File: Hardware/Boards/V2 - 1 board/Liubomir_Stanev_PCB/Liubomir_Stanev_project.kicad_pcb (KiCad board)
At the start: 2 copper layers, 145.5 x 73.5 mm, 30 parts, among them J1 Conn_01x03_Pin, J2 Conn_01x03_Pin, J3 Conn_01x02_Pin, J4 Conn_01x03_Pin, J5 Conn_01x03_Pin, J6 Conn_01x02_Pin, U1 GY-8511 UV sensor, U2 TEMT6000, U3 DS18B20-air, U4 Turbidity sensor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

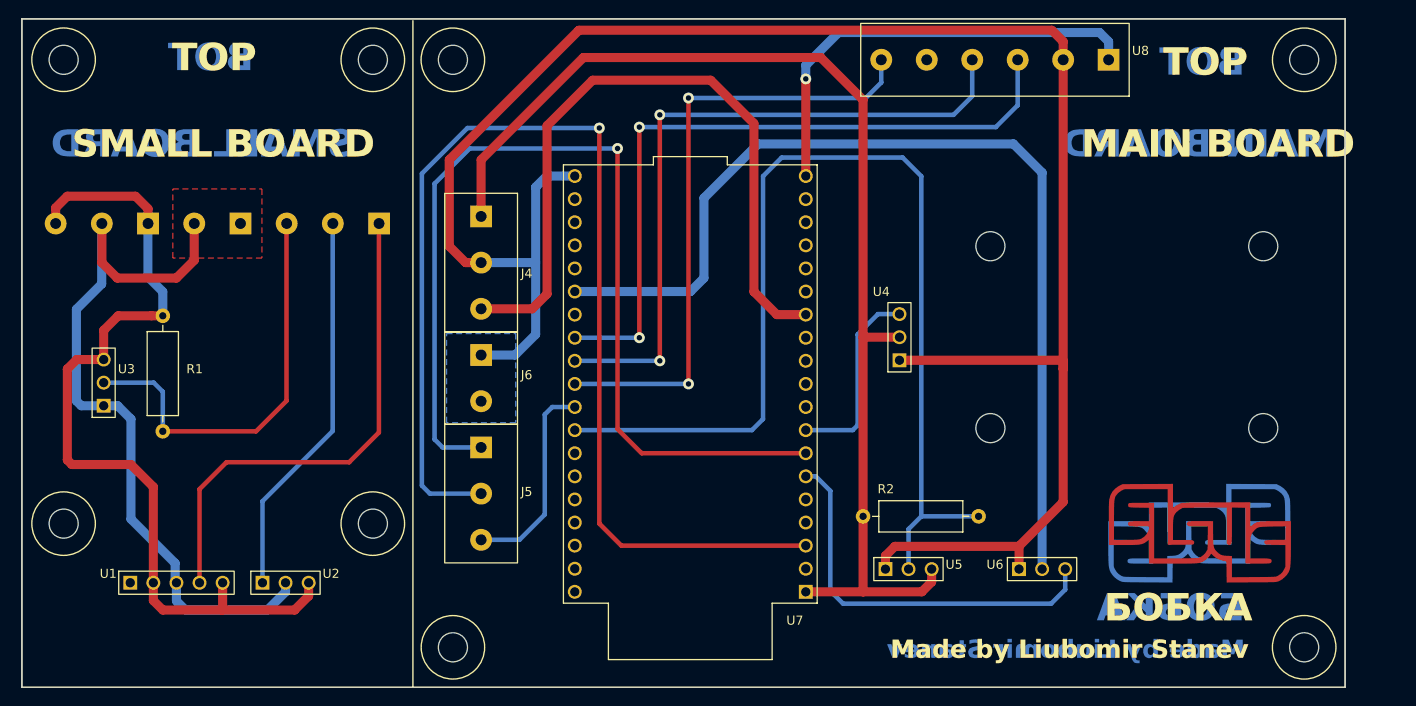
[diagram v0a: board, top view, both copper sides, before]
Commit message: Fixed some issues on the board and addded some logic for the turbidity sensor
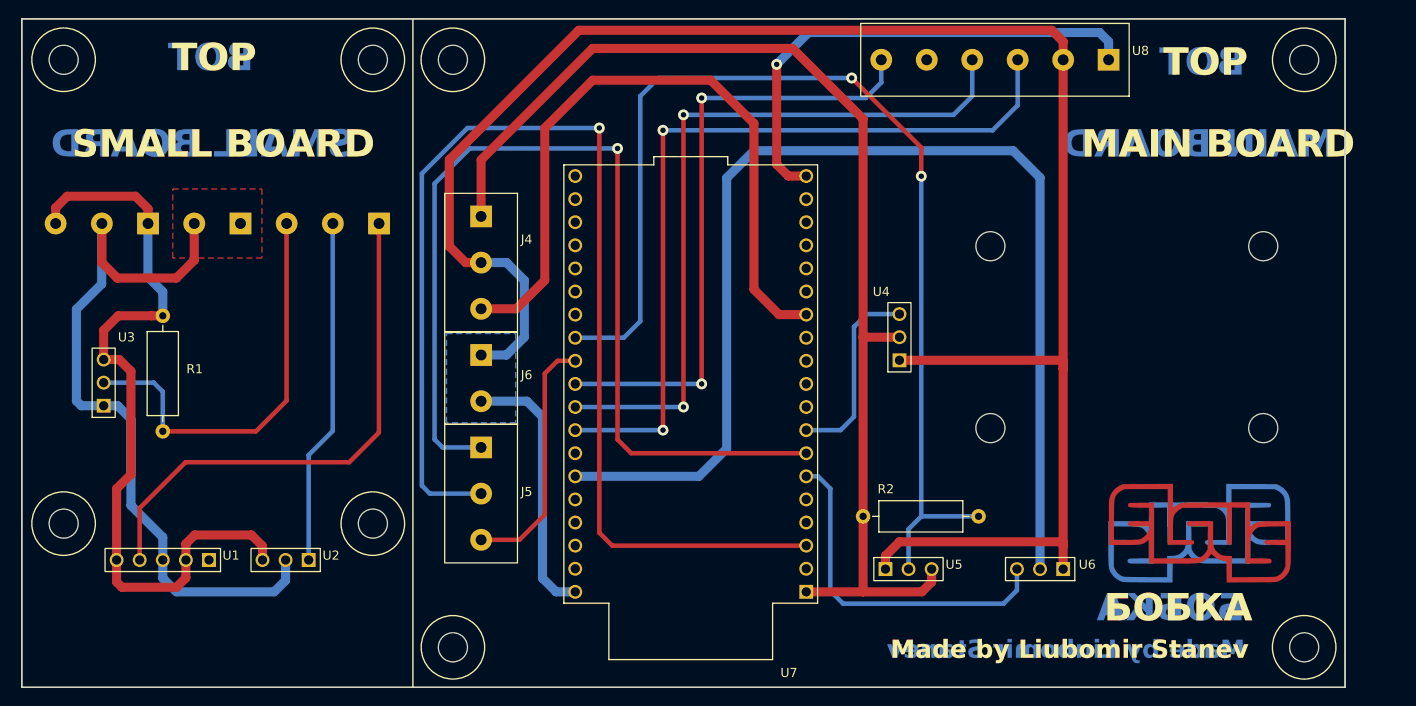
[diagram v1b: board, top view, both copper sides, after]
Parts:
- moved U1 2.92 mm to (66.0, 100.0), turned to 180 degrees
- moved U2 2.50 mm to (79.5, 100.0), turned to 180 degrees
- moved U6 0.23 mm to (162.5, 101.0), turned to 180 degrees
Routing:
- net /water_level_power: track 108.2 -> 127.6 mm
- net GND: track 217.1 -> 233.0 mm
- net +3V3: track 96.1 -> 86.1 mm
- net /relay_brightness_lamp: track 77.9 -> 87.8 mm
- net +5V: track 49.4 -> 55.1 mm
- net /water_level: track 43.7 -> 38.5 mm
- net /air_temp_main: track 22.8 -> 27.6 mm
- net /brightness_out: track 42.7 -> 38.1 mm
- net /relay_uv_lamp: track 75.7 -> 80.3 mm
- net /water_temp: track 117.1 -> 120.8 mm, vias 0 -> 2
- net /uv_out: track 55.6 -> 58.4 mm
- net /uv_ref_main: track 78.5 -> 77.3 mm
- net /uv_out_main: track 108.0 -> 108.6 mm
- net /brightness_out_main: track 130.0 -> 130.6 mm
- net GND1: track 83.9 -> 83.3 mm
